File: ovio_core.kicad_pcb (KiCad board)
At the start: 6 copper layers, 98 x 27.5 mm, 195 parts, among them J101 Conn_01x06, J301 Conn_01x06, J701 USB3_B_Micro, Q501 NTZD3155C, U101 IP4254CZ8-4-TTL, U102 ECP5U_85_CABGA381, U201 TLV62569DRL, U202 TLV62569DRL, U203 TLV62569DRL, U204 TLV62569DRL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

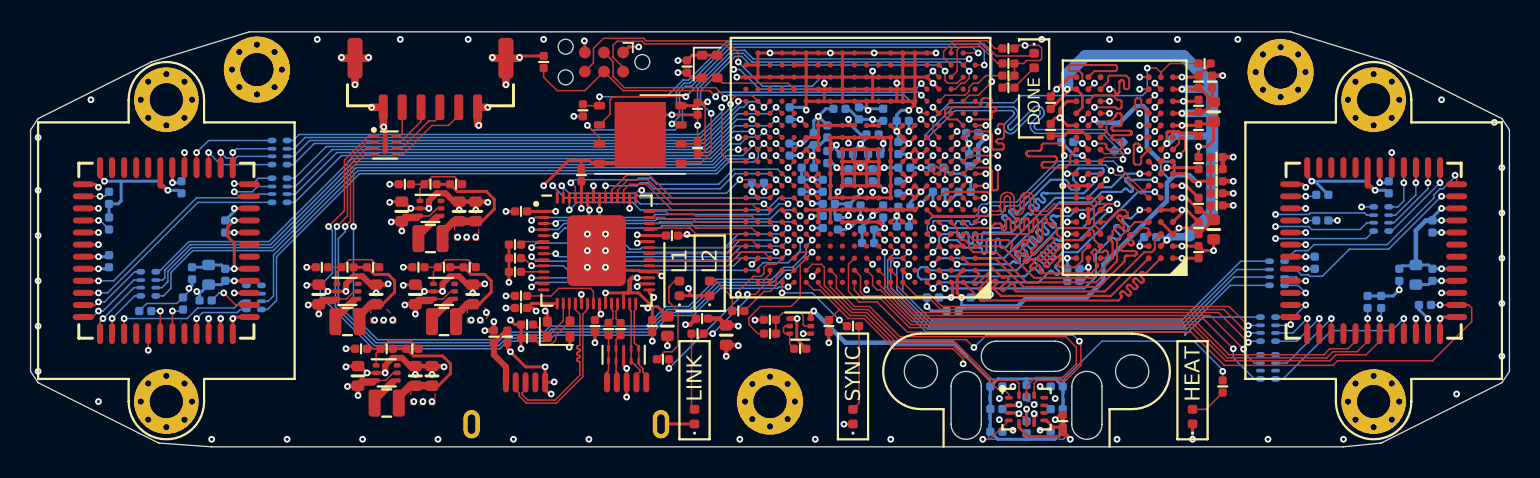
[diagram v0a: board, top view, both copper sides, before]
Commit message: Now with TC2050 for programming
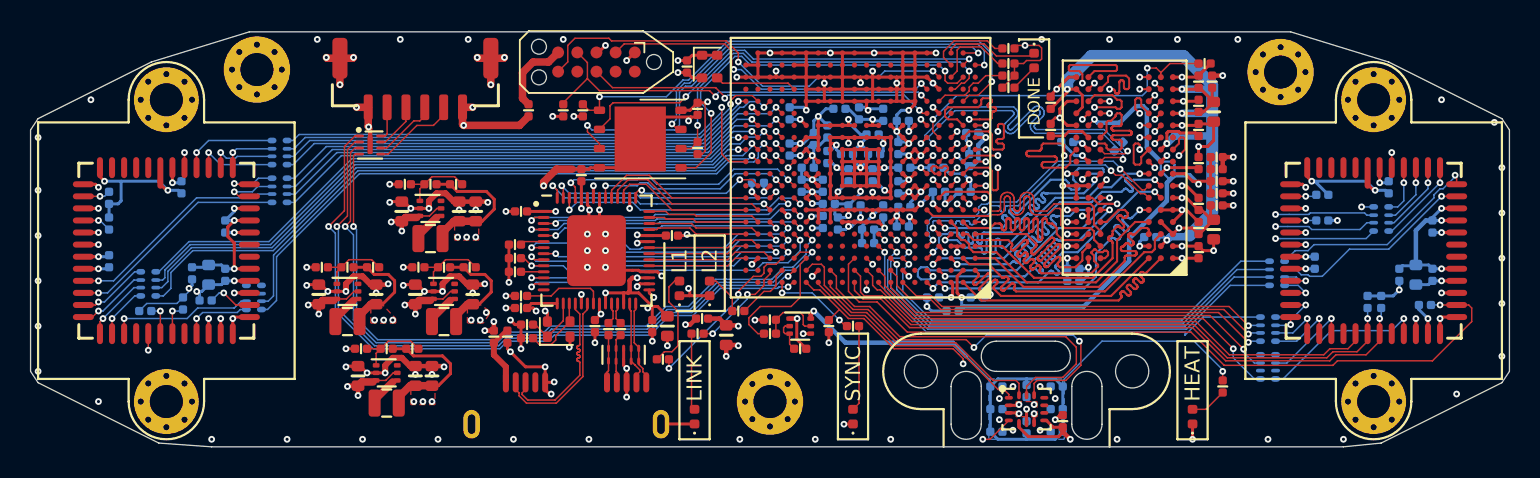
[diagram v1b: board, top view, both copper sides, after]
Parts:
- added R308: 0, passive:R_0402, F.Cu at (181.0, 92.7)
- J301: value Conn_01x06 -> TC2050; footprint Connector:Tag-Connect_TC2030-IDC-NL_2x03_P1.27mm_Vertical -> Connector:Tag-Connect_TC2050-IDC-NL_2x05_P1.27mm_Vertical
- moved R306 3.45 mm to (183.3, 92.7), turned to 270 degrees
- moved J101 1.00 mm to (173.5, 90.5)
- moved U101 1.00 mm to (170.5, 95.0)
- moved J301 0.50 mm to (185.5, 89.5)
- moved U302 0.30 mm to (188.4, 94.6)
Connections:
- J301 pad 3: /FPGA Config/TDI -> GND
- J301 pad 5: GND -> Net-(J301-Pad5)
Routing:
- net Net-(J301-Pad5): track 0.00 -> 5.18 mm
- net +5V: track 86.4 -> 90.0 mm
- net /FPGA Config/TMS: track 25.2 -> 23.1 mm
- net /FPGA Config/TDO: track 27.2 -> 29.0 mm
- net /P_USER_GPIO0: track 47.2 -> 46.1 mm
- net /P_USER_GPIO2: track 48.0 -> 47.1 mm
- net /FPGA Config/TDI: track 23.9 -> 23.3 mm
- net GND: track 350.3 -> 349.6 mm, vias 205 -> 208
- net /P_USER_GPIO1: track 45.8 -> 45.2 mm
- net /P_USER_FLASH_OUT: track 46.3 -> 45.7 mm

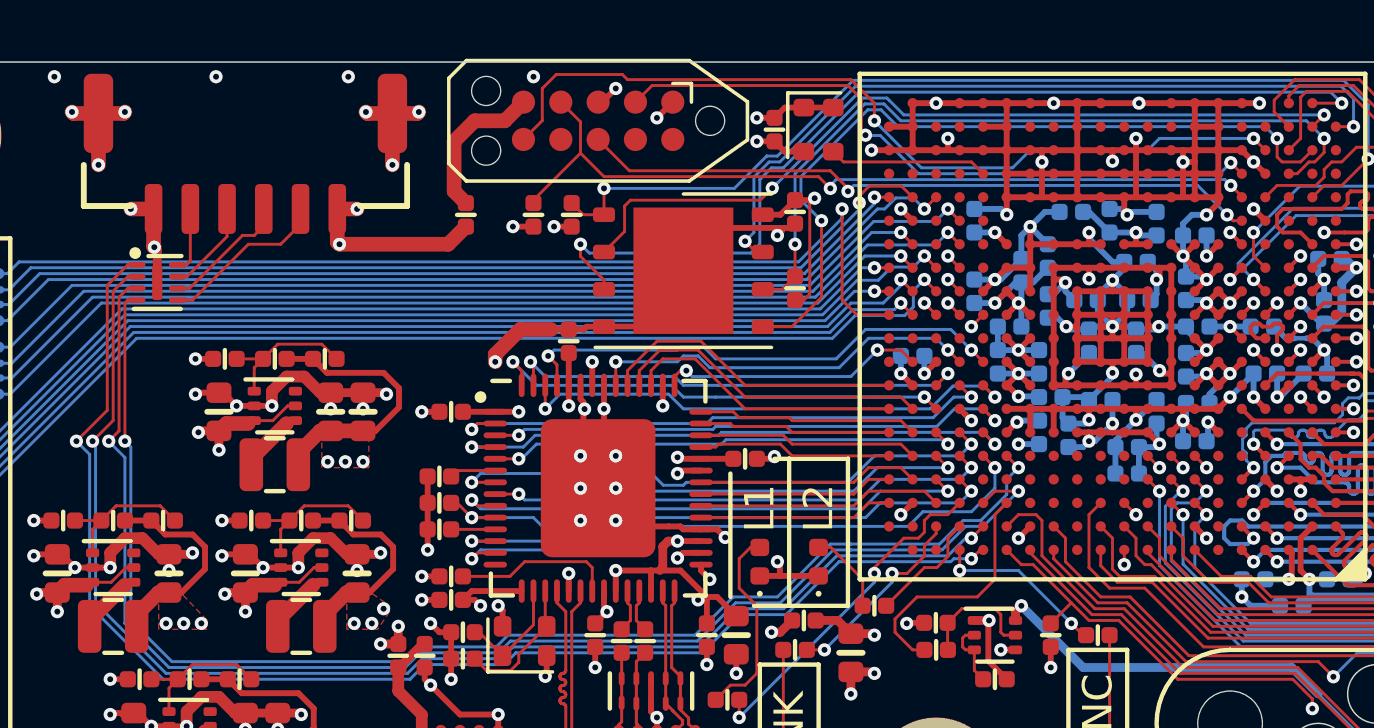
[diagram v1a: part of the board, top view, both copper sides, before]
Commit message: Small cleanup for PCB order
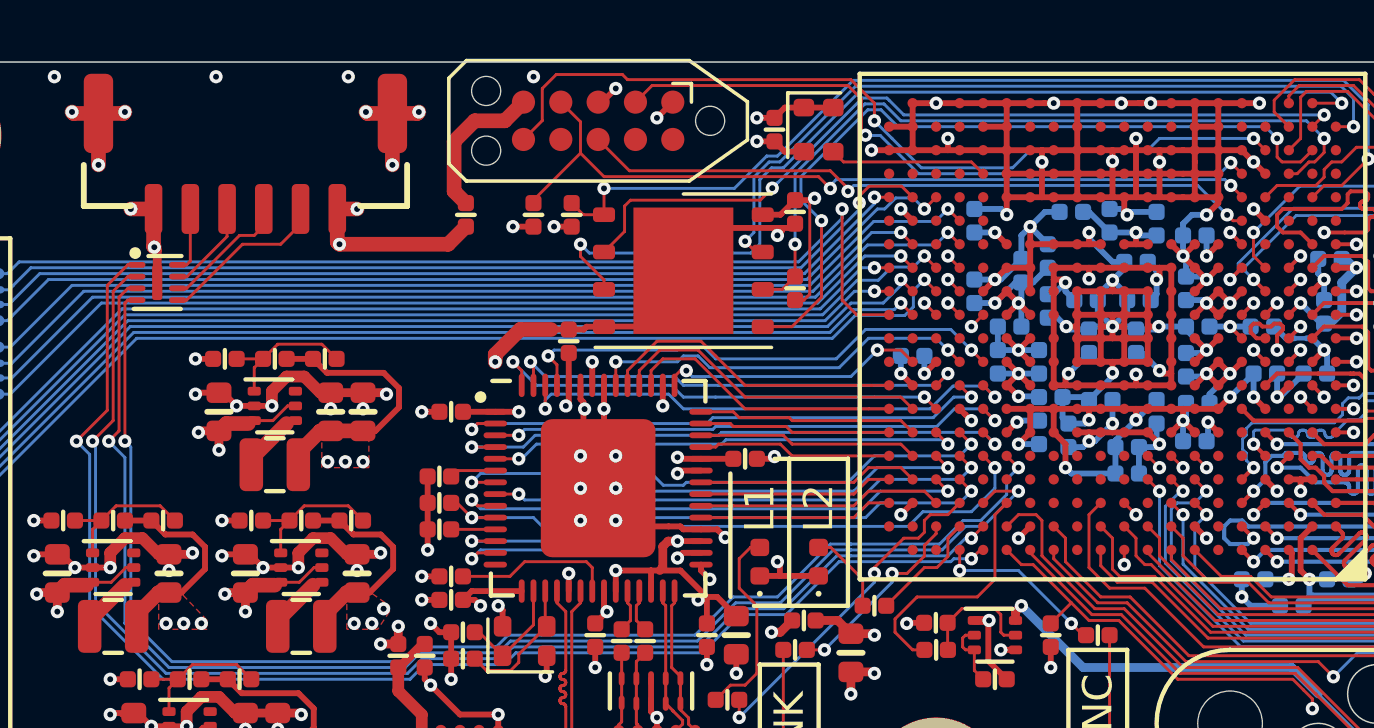
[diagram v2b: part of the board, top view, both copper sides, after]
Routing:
- net GND: track 349.6 -> 353.9 mm, vias 208 -> 210

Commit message: Updated from v1.0 build
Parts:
- R201, R204: value ~ -> 100k
- R202: value ~ -> 120k
- R203: value ~ -> 150k
- R205: value ~ -> 261k
- R206, R208: value ~ -> 82k
- R207: value ~ -> 365k
- turned Q501 to 180 degrees
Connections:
- Q501 pad 1: +5V -> GND
- Q501 pad 2: /Heated IMU/HEATER_BASE -> /Heated IMU/HEATER_SIG
- Q501 pad 3: /Heated IMU/HEATER_BASE -> /Heated IMU/IMU_HEATER
- Q501 pad 4: GND -> +5V
- Q501 pad 5: /Heated IMU/HEATER_SIG -> /Heated IMU/HEATER_BASE
- Q501 pad 6: /Heated IMU/IMU_HEATER -> /Heated IMU/HEATER_BASE
- U102 pad R2: Net-(U102-PadR2) -> /FPGA Config/SPI_CS
- U102 pad T2: /FPGA Config/SPI_CS -> Net-(U102-PadT2)
- U102 pad V2: /FPGA Config/SPI_MOSI -> /FPGA Config/SPI_MISO
- U102 pad W2: /FPGA Config/SPI_MISO -> /FPGA Config/SPI_MOSI
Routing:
- net /FPGA Config/SPI_MISO: track 28.0 -> 32.8 mm
- net /FPGA Config/SPI_MOSI: track 26.4 -> 29.2 mm
- net +1V1: track 32.9 -> 34.6 mm
- net /FPGA Config/SPI_CS: track 34.3 -> 35.0 mm
- net /DDR3 Memory/RESET_N: track 21.9 -> 21.5 mm, vias 2 -> 3
- net GND: track 353.9 -> 353.8 mm, vias 210 -> 209
- net (no net): vias 0 -> 1
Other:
- board text added: "Hardware version: 1.1"
- board text removed: "Hardware version: 1.0"
